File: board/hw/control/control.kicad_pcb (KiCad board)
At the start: 2 copper layers, 54.3 x 82.5 mm, 41 parts, among them J1 stepper #1, J2 stepper #2, J3 buttons, J4 power, J6 AVR-ISP-10, Q1 MMFTP84W, Q2 MMFTP84W, U1 ULN2003A, U2 ULN2003A, U3 ULN2003A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

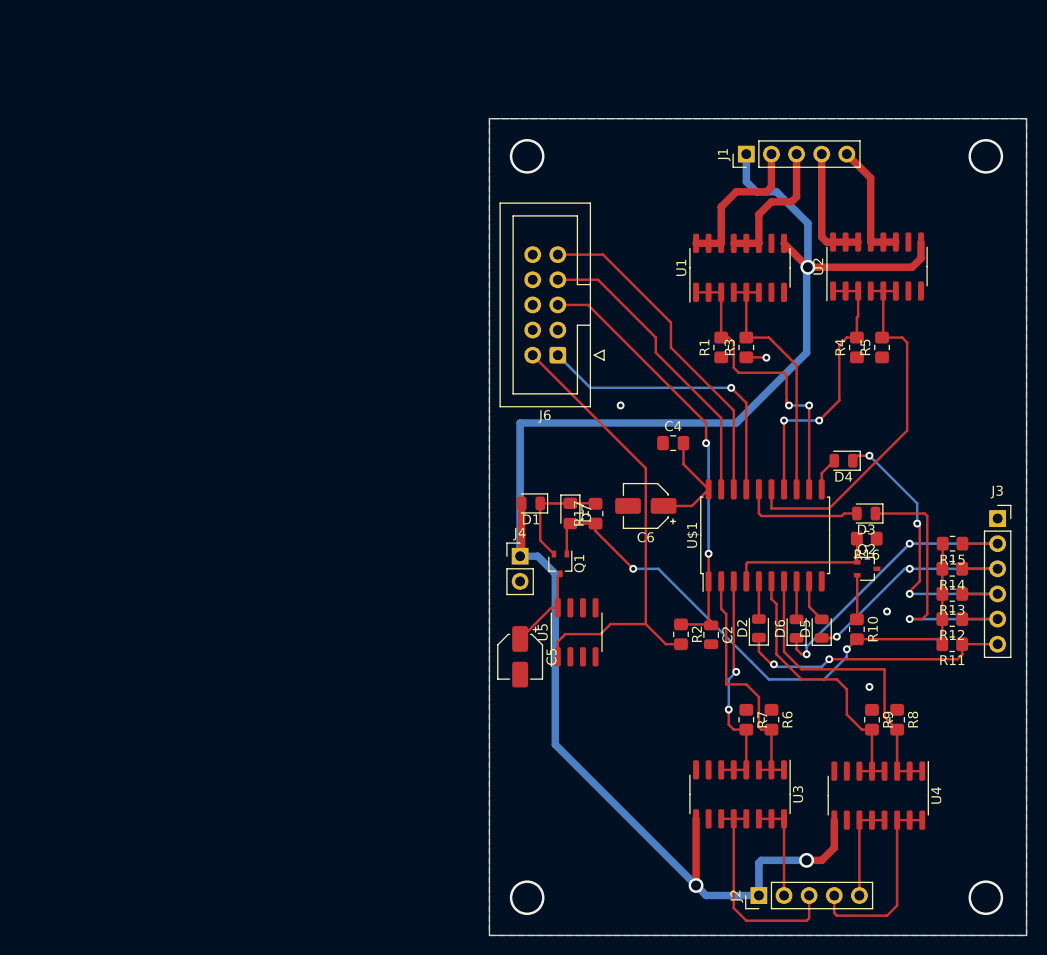
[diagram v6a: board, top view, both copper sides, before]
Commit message: fixed all DRC errors and most warnings
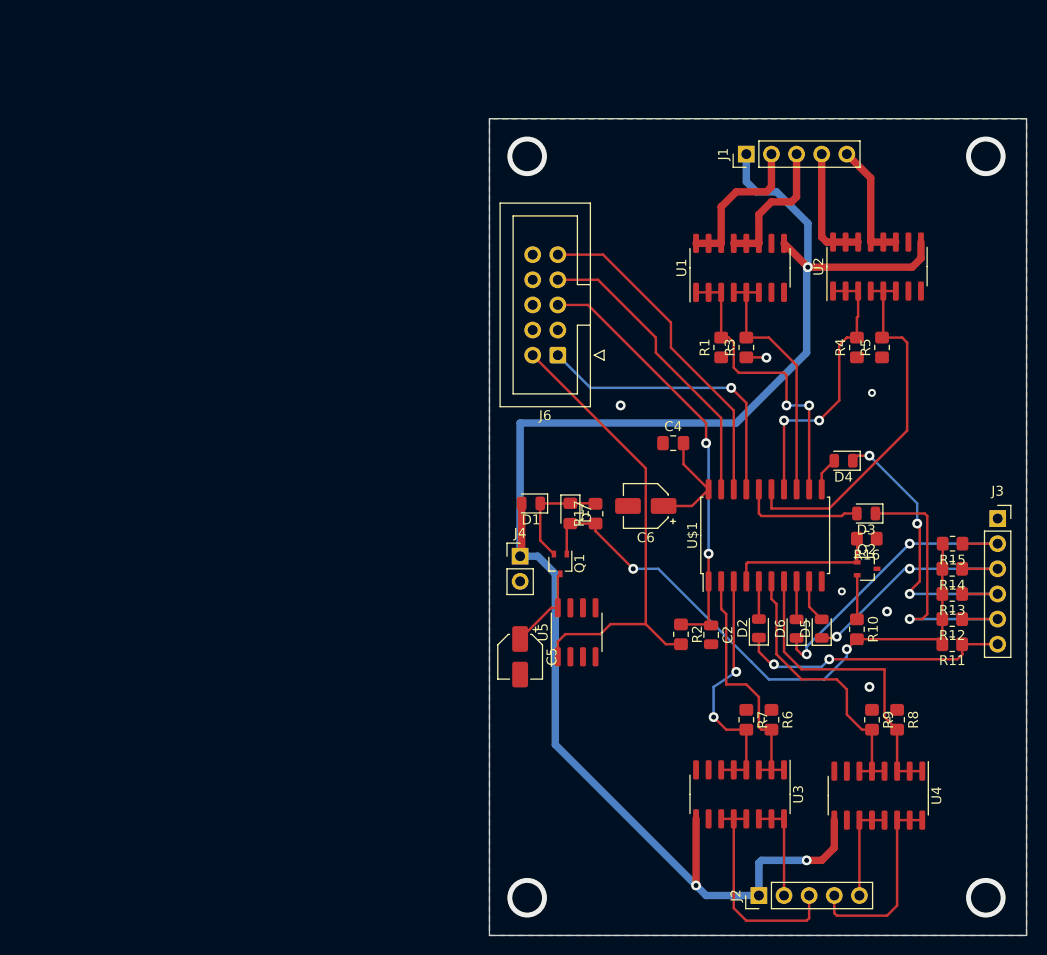
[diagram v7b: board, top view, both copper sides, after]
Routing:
- net Net-(U$1-(TXD)PD1): track 23.5 -> 25.5 mm
- net 0V: track 2.05 -> 2.33 mm, vias 8 -> 10

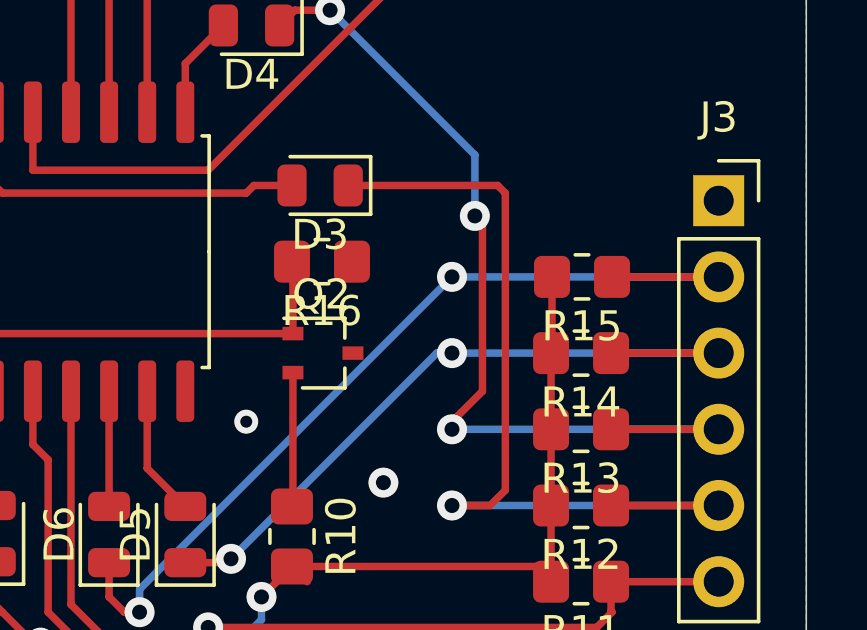
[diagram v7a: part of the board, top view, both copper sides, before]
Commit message: no more warnings + realigned some silkscreens
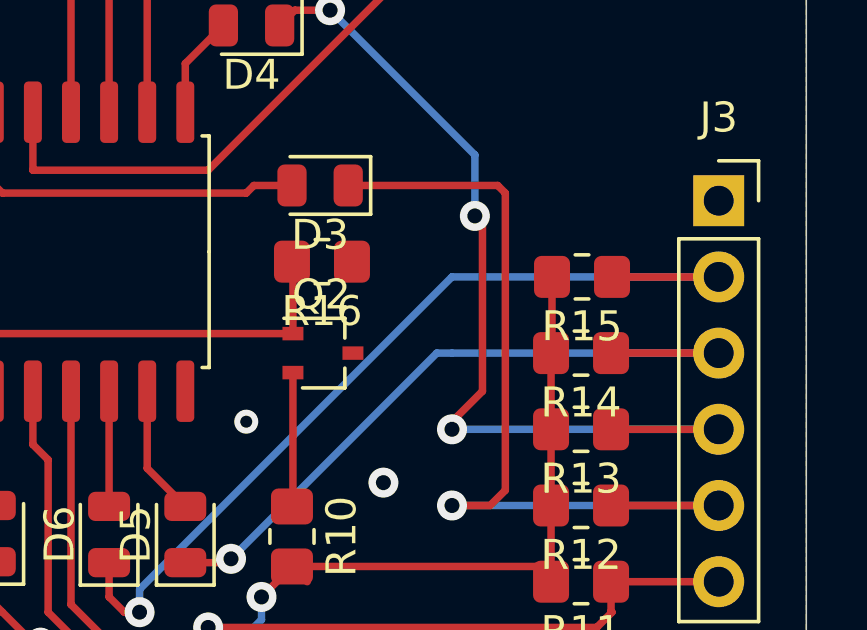
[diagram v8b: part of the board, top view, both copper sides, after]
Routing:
- net Net-(D6-K): vias 2 -> 1
- net Net-(D5-K): vias 2 -> 1
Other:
- board text added: "Lemur's Bobik control board v2.0"
- board text removed: "Lemur's Bobik control board v1.0"
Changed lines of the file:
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@@
         (effects (font (size 1 1) (thickness 0.15)))
     )
-    (fp_text value "AVR-ISP-10" (at 1.27 16.26) (layer "F.Fab")
+    (fp_text value "AVR-ISP-10" (at -4.826 5.334 90) (layer "F.Fab")
         (effects (font (size 1 1) (thickness 0.15)))
     )
@@
         (effects (font (size 1 1) (thickness 0.15)))
     )
-    (fp_text value "4.7µF" (at 0 3.2 90) (layer "F.Fab")
+    (fp_text value "4.7µF" (at 6.096 0 90) (layer "F.Fab")
         (effects (font (size 1 1) (thickness 0.15)))
     )
@@
         (effects (font (size 1 1) (thickness 0.15)))
     )
-    (fp_text value "stepper #2" (at 0 12.49 90) (layer "F.Fab")
+    (fp_text value "stepper #2" (at -2.794 5.588 180) (layer "F.Fab")
         (effects (font (size 1 1) (thickness 0.15)))
     )
@@
         (effects (font (size 1 1) (thickness 0.15)))
     )
-    (fp_text value "stepper #1" (at 0 12.49 90) (layer "F.Fab")
+    (fp_text value "stepper #1" (at 2.794 4.826) (layer "F.Fab")
         (effects (font (size 1 1) (thickness 0.15)))
     )
@@
   (gr_line (start 121.3611 63.7336) (end 121.3611 146.2736)
     (stroke (width 0.05) (type solid)) (layer "Edge.Cuts"))
-  (gr_text "Lemur's Bobik\ncontrol board\nv1.0" (at 118.11 138.43 90) (layer "F.Fab")
+  (gr_text "Lemur's Bobik\ncontrol board\nv2.0" (at 136.906 141.478 90) (layer "F.Fab")
     (effects (font (size 1.63576 1.63576) (thickness 0.14224)) (justify left bottom))
   )
@@
   (segment (start 154.94 116.205) (end 156.337 116.205) (width 0.25) (layer "F.Cu") (net 40))
   (via (at 156.464 116.078) (size 1) (drill 0.5) (layers "F.Cu" "B.Cu") (net 40))
-  (via (at 163.83 109.22) (size 1) (drill 0.5) (layers "F.Cu" "B.Cu") (net 40))
   (segment (start 172.72 109.22) (end 163.83 109.22) (width 0.25) (layer "B.Cu") (net 40))
+  (segment (start 163.83 109.22) (end 163.322 109.22) (width 0.25) (layer "B.Cu") (net 40))
   (segment (start 156.464 116.078) (end 163.322 109.22) (width 0.25) (layer "B.Cu") (net 40))
-  (segment (start 163.322 109.22) (end 163.83 109.22) (width 0.25) (layer "B.Cu") (net 40))
   (segment (start 154.94 114.33) (end 153.67 113.06) (width 0.25) (layer "F.Cu") (net 41))
   (segment (start 153.67 113.06) (end 153.67 110.49) (width 0.25) (layer "F.Cu") (net 41))
@@
   (segment (start 153.416 117.856) (end 152.908 117.856) (width 0.25) (layer "F.Cu") (net 42))
   (segment (start 169.164 106.68) (end 172.72 106.68) (width 0.25) (layer "F.Cu") (net 42))
-  (via (at 163.83 106.68) (size 1) (drill 0.5) (layers "F.Cu" "B.Cu") (net 42))
   (via (at 153.416 117.856) (size 1) (drill 0.5) (layers "F.Cu" "B.Cu") (net 42))
   (segment (start 163.83 106.68) (end 153.416 117.094) (width 0.25) (layer "B.Cu") (net 42))
